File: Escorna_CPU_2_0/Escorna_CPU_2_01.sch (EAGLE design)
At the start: 60 parts, among them IC1 ULN2803, U2 ESP01, X1 AK550/2

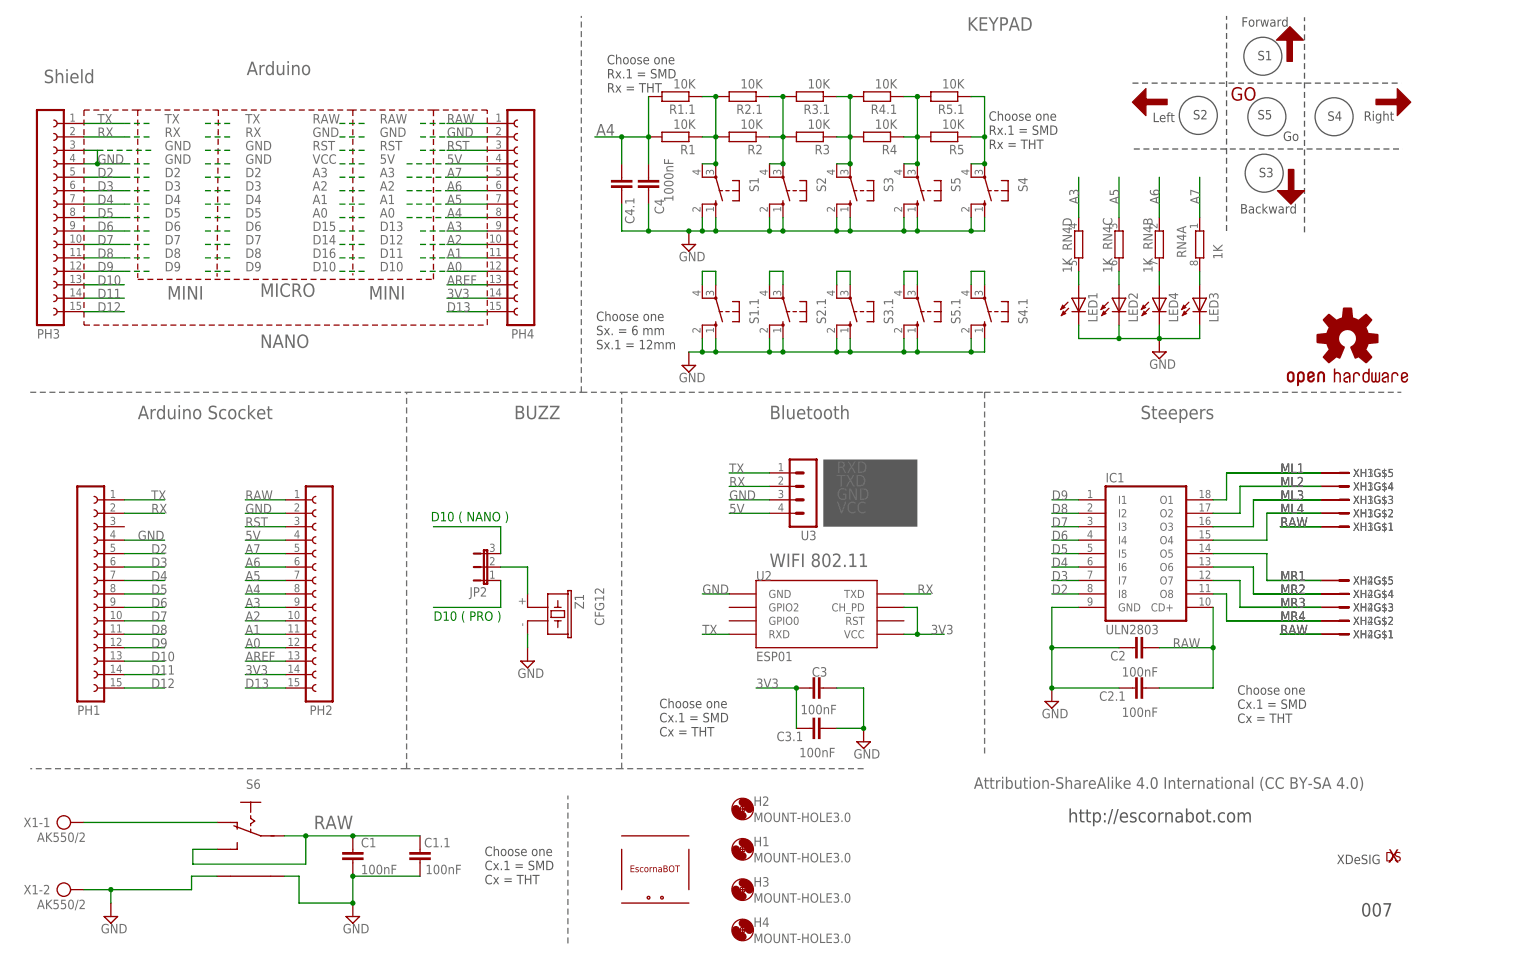
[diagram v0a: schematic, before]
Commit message: error in layer top resolve
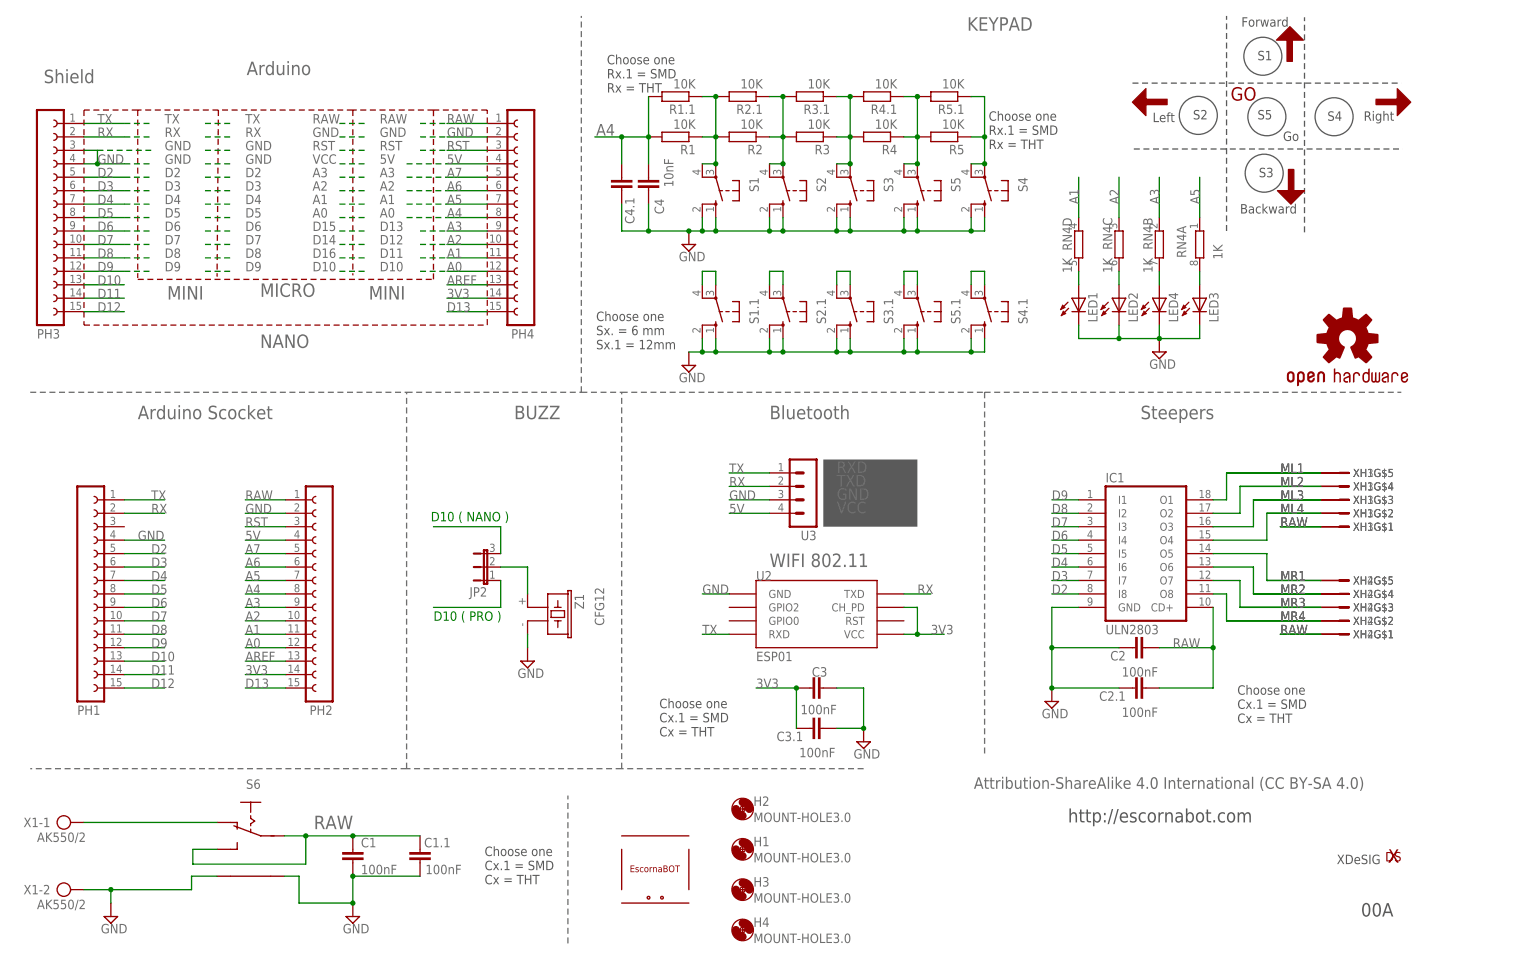
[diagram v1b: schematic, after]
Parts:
- C4: value 1000nF -> 10nF
- C4.1: value 100nF -> 10nF
- S1.1, S2.1, S3.1, S4.1, S5.1: device switch-omron:40-XX -> Escorna_CPU_2_01:SWITCH-OMRON_40-XX
- renumbered LOGO1 to LOGO2, U$10 to U$2, U$4 to U$6, U$7 to U$3, U$8 to U$11, U$9 to U$1
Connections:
- net A1: now also RN4D.1
- net A2: now also RN4C.1
- net A3: now also RN4B.1; no longer RN4D.1
- net A5: now also RN4A.1; no longer RN4C.1
- net A6: no longer RN4B.1
- net A7: no longer RN4A.1
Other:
- note added: "00A"
- note removed: "007"

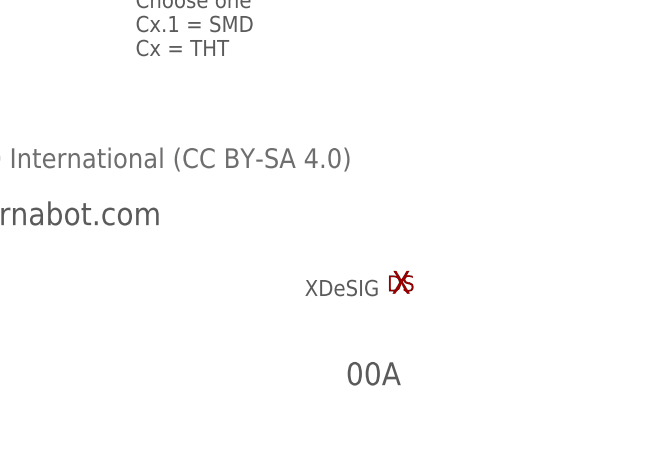
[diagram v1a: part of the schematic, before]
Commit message: Act S6 library
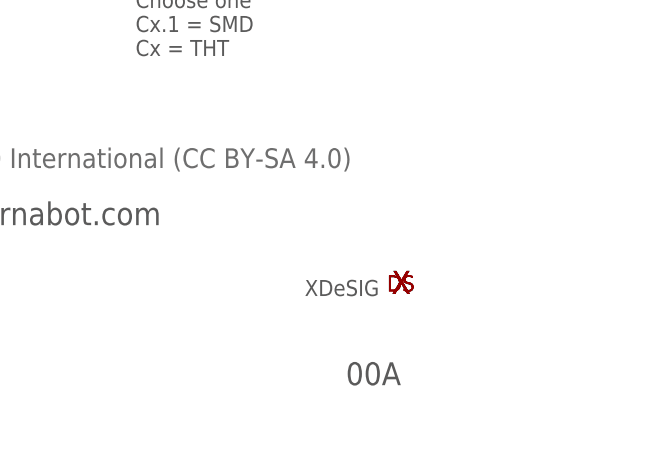
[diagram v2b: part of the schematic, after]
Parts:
- added U$12: XDESIG_XDESIG21, Escorna_CPU_2_01:XDESIG_XDESIG21
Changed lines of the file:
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@@
 <part name="S2.1" library="Escorna_CPU_2_01" deviceset="SWITCH-OMRON_40-XX" device=""/>
 <part name="S1.1" library="Escorna_CPU_2_01" deviceset="SWITCH-OMRON_40-XX" device=""/>
+<part name="U$12" library="Escorna_CPU_2_01" deviceset="XDESIG_XDESIG" device="21"/>
 </parts>
 <sheets>
@@
 <instance part="S2.1" gate="1" x="144.78" y="121.92" rot="R180"/>
 <instance part="S1.1" gate="1" x="132.08" y="121.92" rot="R180"/>
+<instance part="U$12" gate="G$1" x="259.08" y="17.78"/>
 </instances>
 <busses>
